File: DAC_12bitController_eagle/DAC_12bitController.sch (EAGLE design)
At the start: 41 parts, among them IC1 7805T, IC2 79xxT, U1 AD7945BNZ, U2 AD7945BNZ, U3 OP27GZ, U4 OP27GZ, U5 SN74LVC244AN, X1 22-23-2031, X2 22-23-2021, X3 22-23-2021, X4 22-23-2021, X5 22-23-2021, X6 22-23-2021, X7 22-23-2021, X8 22-23-2021, X9 22-23-2021

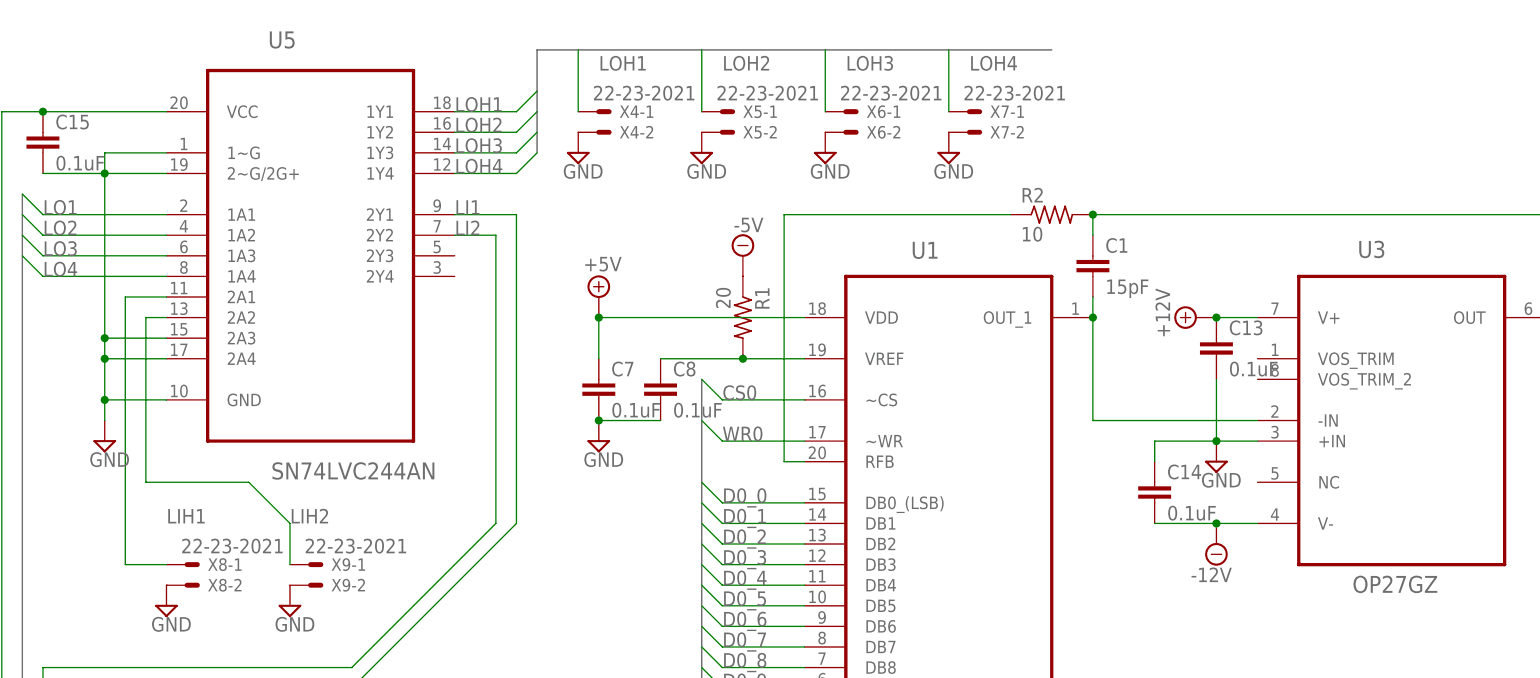
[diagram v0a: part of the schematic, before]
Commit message: Big update to logic flow
Breakout board design for DACs significantly updated to have in-series
impedance and better ground shepherd plane under logic lines. Focused on
design for AD7945 for 2 MHz updates.

FPGA design code expands memory to allow ~69 seconds of waveform data,
external logic triggers to run each channel, and an op-code for a "free
run" mode for the DAC in which it continues to repeat the first waveform
in memory forever.
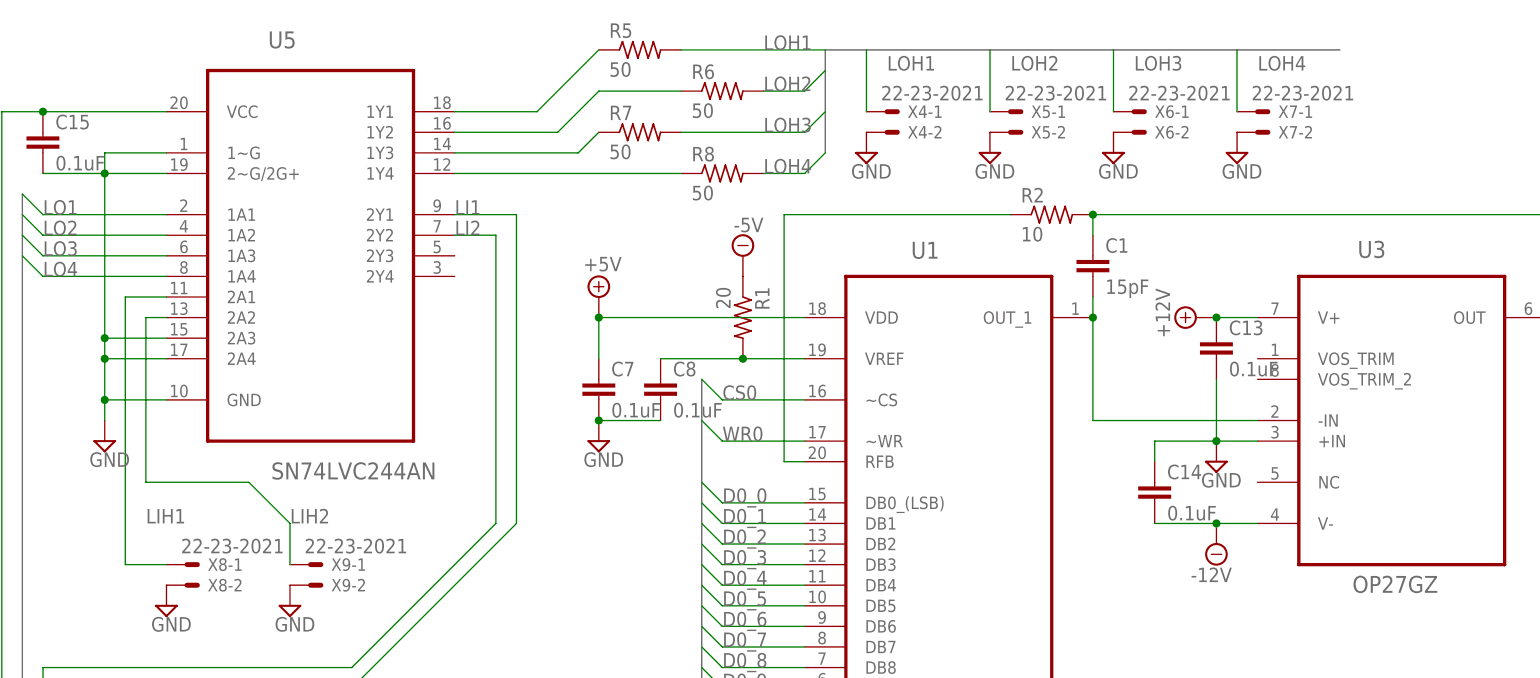
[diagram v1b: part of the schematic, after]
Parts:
- added R5, R6, R7, R8: 50, resistor:R-US_0207/10
- R1, R2, R3, R4: device rcl:R-US_0207/12 -> resistor:R-US_0207/10
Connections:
- new net N$5: R5.1, U5.1Y1
- new net N$6: R6.1, U5.1Y2
- new net N$7: R7.1, U5.1Y3
- new net N$8: R8.1, U5.1Y4
- net LOH1: now also R5.2; no longer U5.1Y1
- net LOH2: now also R6.2; no longer U5.1Y2
- net LOH3: now also R7.2; no longer U5.1Y3
- net LOH4: now also R8.2; no longer U5.1Y4
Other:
- moved on the sheet: X4-1, X4-2, X5-1, X5-2, X6-1, X6-2, X7-1, X7-2
